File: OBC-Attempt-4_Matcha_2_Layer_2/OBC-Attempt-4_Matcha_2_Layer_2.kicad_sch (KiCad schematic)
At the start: 46 parts, among them J2 Screw_Terminal_01x08, J5 Conn_01x04, J6 Micro_SD_Card, J7 Screw_Terminal_01x02, J8 Screw_Terminal_01x02, SW1 PCM12SMTR, U1 BMI088, U12 NCP1117-3.3_SOT223, U2 CPC1020NTR, U3 CPC1020NTR, U4 CPC1020NTR, U5 CPC1020NTR, U9 STM32F401RDTx, Y1 ABMM2-25MHZ-D1-T

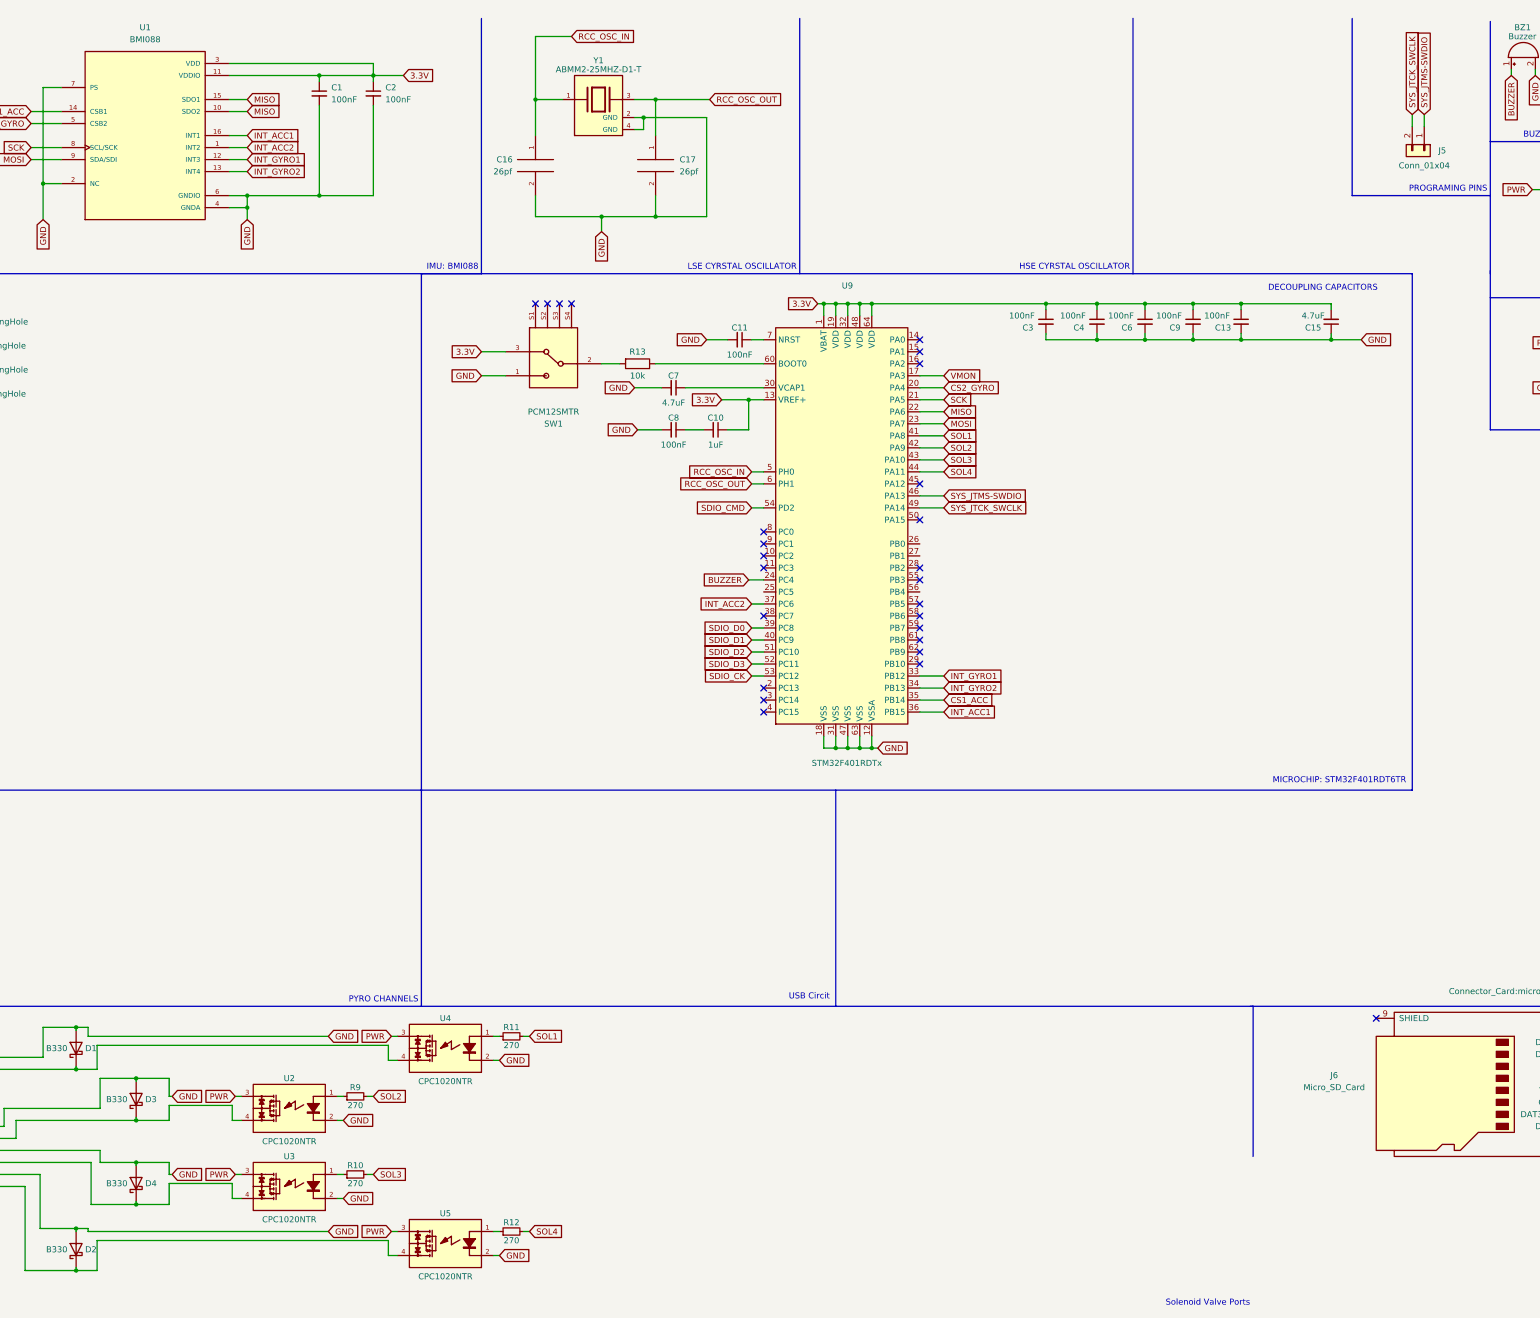
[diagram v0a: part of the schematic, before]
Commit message: 1x4 prog pins
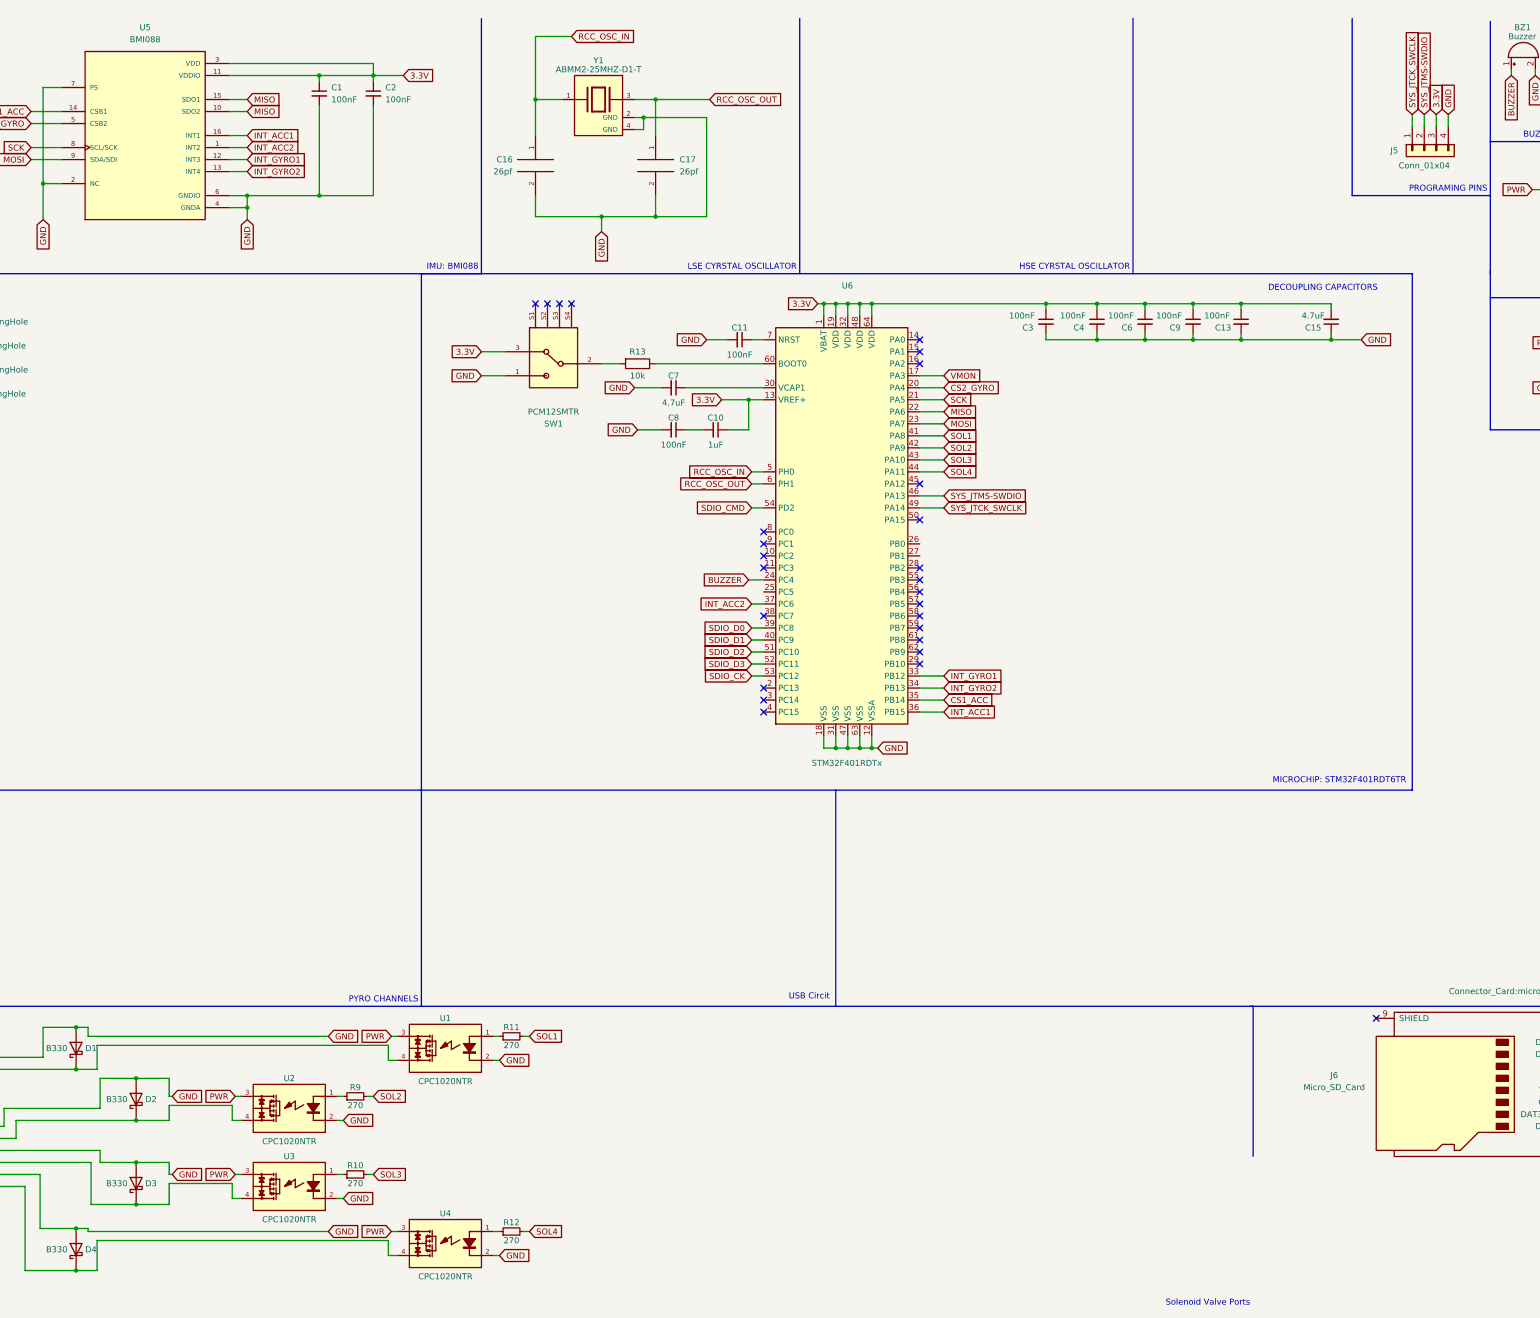
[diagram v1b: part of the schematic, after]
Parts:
- J5: footprint Connector_PinHeader_2.54mm:PinHeader_1x02_P2.54mm_Vertical -> Connector_PinHeader_2.54mm:PinHeader_1x04_P2.54mm_Vertical; symbol Connector_Generic:Conn_01x02 -> Connector_Generic:Conn_01x04
- renumbered D3 to D2, D4 to D3, D2 to D4, U4 to U1, U5 to U4, U1 to U5, U9 to U6
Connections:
- net 3.3V: now also J5.3 (Pin_3)
- net GND: now also J5.4 (Pin_4)
- net SYS_JTCK_SWCLK: now also J5.1 (Pin_1); no longer J5.2 (Pin_2)
- net SYS_JTMS-SWDIO: now also J5.2 (Pin_2); no longer J5.1 (Pin_1)
- no-connect marks 26 -> 27
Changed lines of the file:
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@@
   (no_connect (at 229.87 146.05))
   (no_connect (at 196.85 123.19))
+  (no_connect (at 229.87 133.35))
   (no_connect (at 196.85 153.67))
   (no_connect (at 153.67 72.39))
@@
     (stroke (width 0) (type default) (color 0 0 0 0))
   )
+  (wire (pts (xy 336.55 32.385) (xy 336.55 34.925))
+    (stroke (width 0) (type default) (color 0 0 0 0))
+  )
   (wire (pts (xy 148.59 36.83) (xy 148.59 29.21))
     (stroke (width 0) (type default) (color 0 0 0 0))
@@
     (stroke (width 0) (type default) (color 0 0 0 0))
   )
-  (wire (pts (xy 336.55 32.385) (xy 336.55 34.925))
-    (stroke (width 0) (type default) (color 0 0 0 0))
-  )
   (wire (pts (xy 117.475 229.235) (xy 55.88 229.235))
     (stroke (width 0) (type default) (color 0 0 0 0))
@@
     (stroke (width 0) (type default) (color 0 0 0 0))
   )
+  (wire (pts (xy 334.01 32.385) (xy 334.01 34.925))
+    (stroke (width 0) (type default) (color 0 0 0 0))
+  )
+  (wire (pts (xy 339.09 32.385) (xy 339.09 34.925))
+    (stroke (width 0) (type default) (color 0 0 0 0))
+  )
   (polyline (pts (xy 274.955 12.065) (xy 274.955 66.04))
     (stroke (width 0) (type default) (color 0 0 0 0))
@@
     (stroke (width 0) (type default) (color 0 0 0 0))
   )
-  (wire (pts (xy 334.01 32.385) (xy 334.01 34.925))
-    (stroke (width 0) (type default) (color 0 0 0 0))
-  )
   (wire (pts (xy 43.815 267.97) (xy 51.435 267.97))
     (stroke (width 0) (type default) (color 0 0 0 0))
@@
   )
   (wire (pts (xy 71.755 240.03) (xy 71.12 240.03))
+    (stroke (width 0) (type default) (color 0 0 0 0))
+  )
+  (wire (pts (xy 341.63 32.385) (xy 341.63 34.925))
     (stroke (width 0) (type default) (color 0 0 0 0))
   )
@@
     )
   )
+  (global_label "GND" (shape input) (at 341.63 32.385 90) (fields_autoplaced)
+    (effects (font (size 1.27 1.27)) (justify left))
+    (property "Intersheet References" "${INTERSHEET_REFS}" (id 0) (at 341.7094 26.1014 90)
+      (effects (font (size 1.27 1.27)) (justify left) hide)
+    )
+  )
   (global_label "GND" (shape input) (at 44.45 54.61 270) (fields_autoplaced)
     (effects (font (size 1.27 1.27)) (justify right))
@@
     )
   )
+  (global_label "3.3V" (shape input) (at 339.09 32.385 90) (fields_autoplaced)
+    (effects (font (size 1.27 1.27)) (justify left))
+    (property "Intersheet References" "${INTERSHEET_REFS}" (id 0) (at 339.0106 25.8595 90)
+      (effects (font (size 1.27 1.27)) (justify left) hide)
+    )
+  )
   (symbol (lib_id "Diode:B330") (at 64.135 258.445 90) (unit 1)
     (in_bom yes) (on_board yes)
-    (property "Reference" "D4" (id 0) (at 66.04 258.445 90)
+    (property "Reference" "D3" (id 0) (at 66.04 258.445 90)
       (effects (font (size 1.27 1.27)) (justify right))
     )
@@
   (symbol (lib_id "CPC1020NTR:CPC1020NTR") (at 129.54 229.87 0) (mirror y) (unit 1)
     (in_bom yes) (on_board yes)
-    (property "Reference" "U4" (id 0) (at 129.54 223.52 0))
+    (property "Reference" "U1" (id 0) (at 129.54 223.52 0))
     (property "Value" "CPC1020NTR" (id 1) (at 129.54 236.855 0))
     (property "Footprint" "CPC1020NTR:4-SOP" (id 2) (at 129.54 229.87 0)
@@
     (pin "2")
   )
-  (symbol (lib_id "Connector_Generic:Conn_01x02") (at 336.55 40.005 270) (unit 1)
-    (in_bom yes) (on_board yes)
-    (property "Reference" "J5" (id 0) (at 340.36 40.005 90))
+  (symbol (lib_id "Connector_Generic:Conn_01x04") (at 336.55 40.005 90) (mirror x) (unit 1)
+    (in_bom yes) (on_board yes)
+    (property "Reference" "J5" (id 0) (at 330.2 40.005 90))
     (property "Value" "Conn_01x04" (id 1) (at 336.55 43.18 90))
-    (property "Footprint" "Connector_PinHeader_2.54mm:PinHeader_1x02_P2.54mm_Vertical" (id 2) (at 336.55 40.005 0)
+    (property "Footprint" "Connector_PinHeader_2.54mm:PinHeader_1x04_P2.54mm_Vertical" (id 2) (at 336.55 40.005 0)
       (effects (font (size 1.27 1.27)) hide)
     )
@@
     (pin "1")
     (pin "2")
+    (pin "3")
+    (pin "4")
   )
   (symbol (lib_id "Connector:Screw_Terminal_01x02") (at 382.27 27.94 0) (unit 1)
@@
   (symbol (lib_id "Diode:B330") (at 64.135 240.665 90) (unit 1)
     (in_bom yes) (on_board yes)
-    (property "Reference" "D3" (id 0) (at 66.04 240.665 90)
+    (property "Reference" "D2" (id 0) (at 66.04 240.665 90)
       (effects (font (size 1.27 1.27)) (justify right))
     )
@@
   (symbol (lib_id "MCU_ST_STM32F4:STM32F401RDTx") (at 214.63 118.11 0) (unit 1)
     (in_bom yes) (on_board yes)
-    (property "Reference" "U9" (id 0) (at 213.36 68.58 0)
+    (property "Reference" "U6" (id 0) (at 213.36 68.58 0)
       (effects (font (size 1.27 1.27)) (justify left))
     )
@@
   (symbol (lib_id "CPC1020NTR:CPC1020NTR") (at 129.54 271.145 0) (mirror y) (unit 1)
     (in_bom yes) (on_board yes)
-    (property "Reference" "U5" (id 0) (at 129.54 264.795 0))
+    (property "Reference" "U4" (id 0) (at 129.54 264.795 0))
     (property "Value" "CPC1020NTR" (id 1) (at 129.54 278.13 0))
     (property "Footprint" "CPC1020NTR:4-SOP" (id 2) (at 129.54 271.145 0)
@@
   (symbol (lib_id "Diode:B330") (at 51.435 272.415 90) (unit 1)
     (in_bom yes) (on_board yes)
-    (property "Reference" "D2" (id 0) (at 53.34 272.415 90)
+    (property "Reference" "D4" (id 0) (at 53.34 272.415 90)
       (effects (font (size 1.27 1.27)) (justify right))
     )
@@
   (symbol (lib_id "BMI088:BMI088") (at 66.04 36.83 0) (unit 1)
     (in_bom yes) (on_board yes) (fields_autoplaced)
-    (property "Reference" "U1" (id 0) (at 66.04 13.97 0))
+    (property "Reference" "U5" (id 0) (at 66.04 13.97 0))
     (property "Value" "BMI088" (id 1) (at 66.04 16.51 0))
     (property "Footprint" "BMI088:BMI088" (id 2) (at 66.04 36.83 0)
@@
       (reference "D1") (unit 1) (value "B330") (footprint "Diode_SMD:D_SMA")
     )
+    (path "/525fe670-153d-4d5b-a25c-974e9d509e14"
+      (reference "D2") (unit 1) (value "B330") (footprint "Diode_SMD:D_SMA")
+    )
+    (path "/00d8d2dc-b75f-4916-b012-c6252281aa16"
+      (reference "D3") (unit 1) (value "B330") (footprint "Diode_SMD:D_SMA")
+    )
     (path "/ca235195-3b48-401a-9188-43007c5ff9fc"
-      (reference "D2") (unit 1) (value "B330") (footprint "Diode_SMD:D_SMA")
-    )
-    (path "/525fe670-153d-4d5b-a25c-974e9d509e14"
-      (reference "D3") (unit 1) (value "B330") (footprint "Diode_SMD:D_SMA")
-    )
-    (path "/00d8d2dc-b75f-4916-b012-c6252281aa16"
       (reference "D4") (unit 1) (value "B330") (footprint "Diode_SMD:D_SMA")
     )
@@
     )
     (path "/35fc0a09-4646-4e07-b775-2a0200b8312f"
-      (reference "J5") (unit 1) (value "Conn_01x04") (footprint "Connector_PinHeader_2.54mm:PinHeader_1x02_P2.54mm_Vertical")
+      (reference "J5") (unit 1) (value "Conn_01x04") (footprint "Connector_PinHeader_2.54mm:PinHeader_1x04_P2.54mm_Vertical")
     )
     (path "/e7690818-e758-46a6-9705-a6bc65e0e656"
@@
       (reference "SW1") (unit 1) (value "PCM12SMTR") (footprint "PCM12SMTR:SW_PCM12SMTR")
     )
-    (path "/d6cf2984-f57f-403a-b8f7-9a965c75371c"
-      (reference "U1") (unit 1) (value "BMI088") (footprint "BMI088:BMI088")
+    (path "/315aec16-27d0-4fe8-b401-b72f67ecbe1b"
+      (reference "U1") (unit 1) (value "CPC1020NTR") (footprint "CPC1020NTR:4-SOP")
     )
     (path "/62abc4e9-c45f-450a-8016-f0148358d373"
@@
       (reference "U3") (unit 1) (value "CPC1020NTR") (footprint "CPC1020NTR:4-SOP")
     )
-    (path "/315aec16-27d0-4fe8-b401-b72f67ecbe1b"
+    (path "/928505cb-ec39-4887-be4b-ad6eba58bf0f"
       (reference "U4") (unit 1) (value "CPC1020NTR") (footprint "CPC1020NTR:4-SOP")
     )
-    (path "/928505cb-ec39-4887-be4b-ad6eba58bf0f"
-      (reference "U5") (unit 1) (value "CPC1020NTR") (footprint "CPC1020NTR:4-SOP")
+    (path "/d6cf2984-f57f-403a-b8f7-9a965c75371c"
+      (reference "U5") (unit 1) (value "BMI088") (footprint "BMI088:BMI088")
     )
     (path "/7f9cfec9-ae4e-4547-b66d-604abafc0c5c"
-      (reference "U9") (unit 1) (value "STM32F401RDTx") (footprint "Package_QFP:LQFP-64_10x10mm_P0.5mm")
+      (reference "U6") (unit 1) (value "STM32F401RDTx") (footprint "Package_QFP:LQFP-64_10x10mm_P0.5mm")
     )
     (path "/4ee65a9e-109d-4983-886b-576cabc08fdf"
